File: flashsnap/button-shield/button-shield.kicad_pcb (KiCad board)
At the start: 2 copper layers, 47 x 11 mm, 8 parts, among them P1 CONN_4, P2 CONN_4, SW1 SW_PUSH, SW2 DUAL_SWITCH_INV

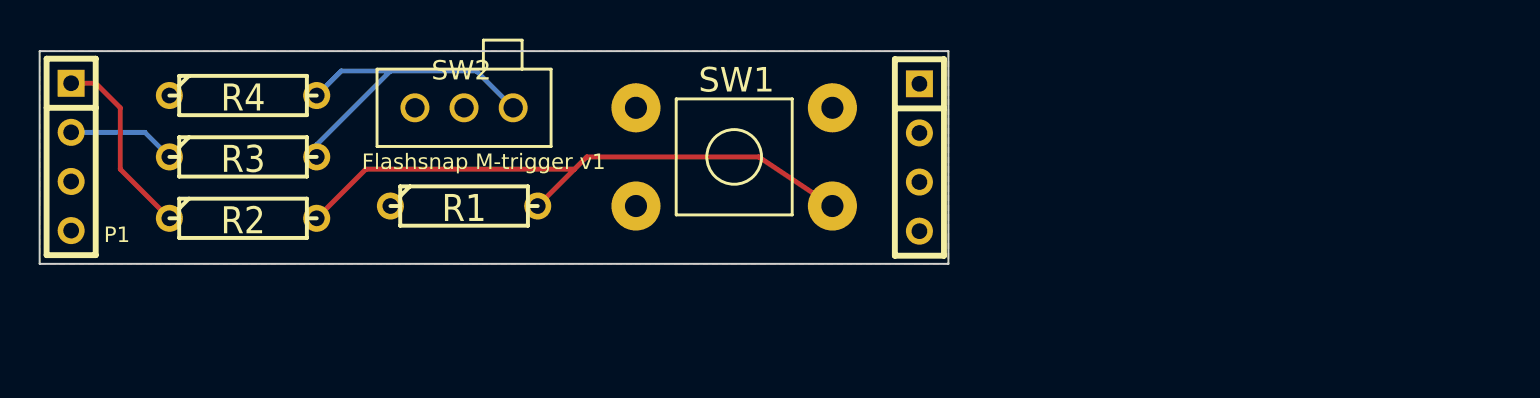
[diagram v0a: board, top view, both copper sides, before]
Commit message: flashsnap: Introduce cable-shield, update others.
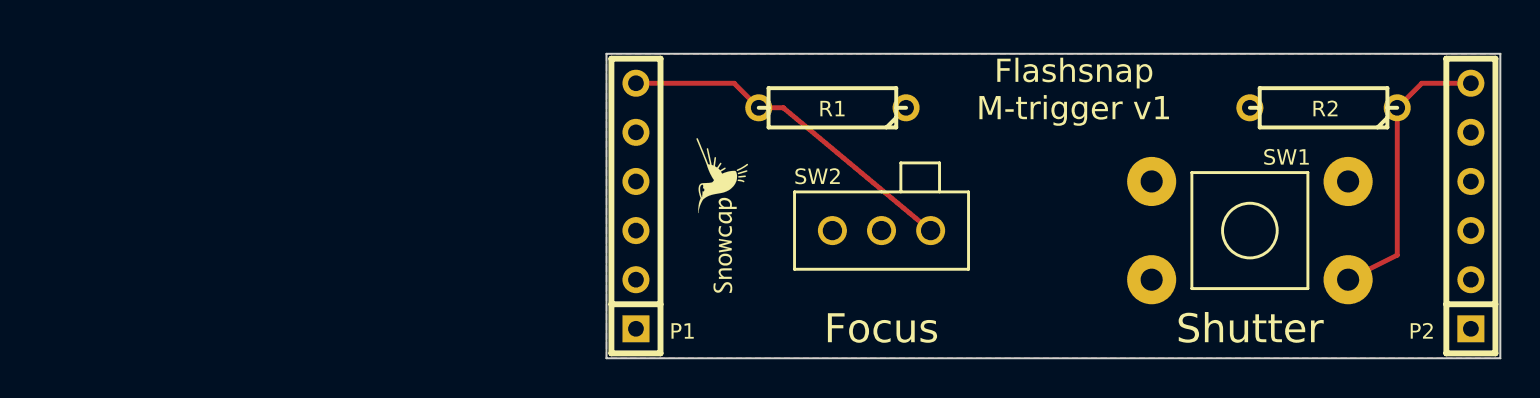
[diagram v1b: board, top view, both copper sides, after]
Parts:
- removed R3, R4: R, R3
- added VAL: REF, LOGO_SMALL_SNOWCAP_FRONT, F.Cu at (184.8, 144.0)
- P1, P2: value CONN_4 -> CONN_6; footprint SIL-4 -> SIL-6
- moved R2 56.2 mm to (215.9, 138.4), turned to 180 degrees
- moved P1 29.3 mm to (180.3, 143.5), turned to 90 degrees
- moved P2 28.6 mm to (223.5, 143.5), turned to 90 degrees
- moved SW1 26.9 mm to (212.1, 144.8)
- moved SW2 22.5 mm to (193.0, 144.8)
- moved R1 19.7 mm to (190.5, 138.4), turned to 180 degrees
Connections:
- P1 pad 1: N-000004 -> N-000008
- P1 pad 2: N-000002 -> N-000006
- P1 pad 3: N-000003 -> (no net)
- P1 pad 4: N-000001 -> (no net)
- R1 pad 1: N-000003 -> N-000008
- R1 pad 2: N-000005 -> N-000001
- R2 pad 1: N-000004 -> N-000005
- R2 pad 2: N-000005 -> N-000008
- SW1 pad 1: N-000001 -> N-000006
- SW2 pad 1: N-000006 -> N-000001
- SW2 pad 2: N-000001 -> N-000006
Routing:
- net N-000001: track 0.00 -> 18.1 mm
- net N-000006: track 17.5 -> 0.00 mm
- net N-000005: track 31.4 -> 14.8 mm
- net N-000004: track 9.83 -> 0.00 mm
- net N-000002: track 5.61 -> 0.00 mm
- added copper zone on B.Cu, net N-000006
- added copper zone on F.Cu, net N-000008
- removed copper zone on F.Cu, net N-000001
- removed copper zone on B.Cu, net N-000003
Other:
- board size 47 x 11 mm -> 46.2 x 15.7 mm
- board text added: "Focus"
- board text added: "Shutter"
